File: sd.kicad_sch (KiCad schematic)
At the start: 2 parts, among them J6 Micro_SD_Card_Det1

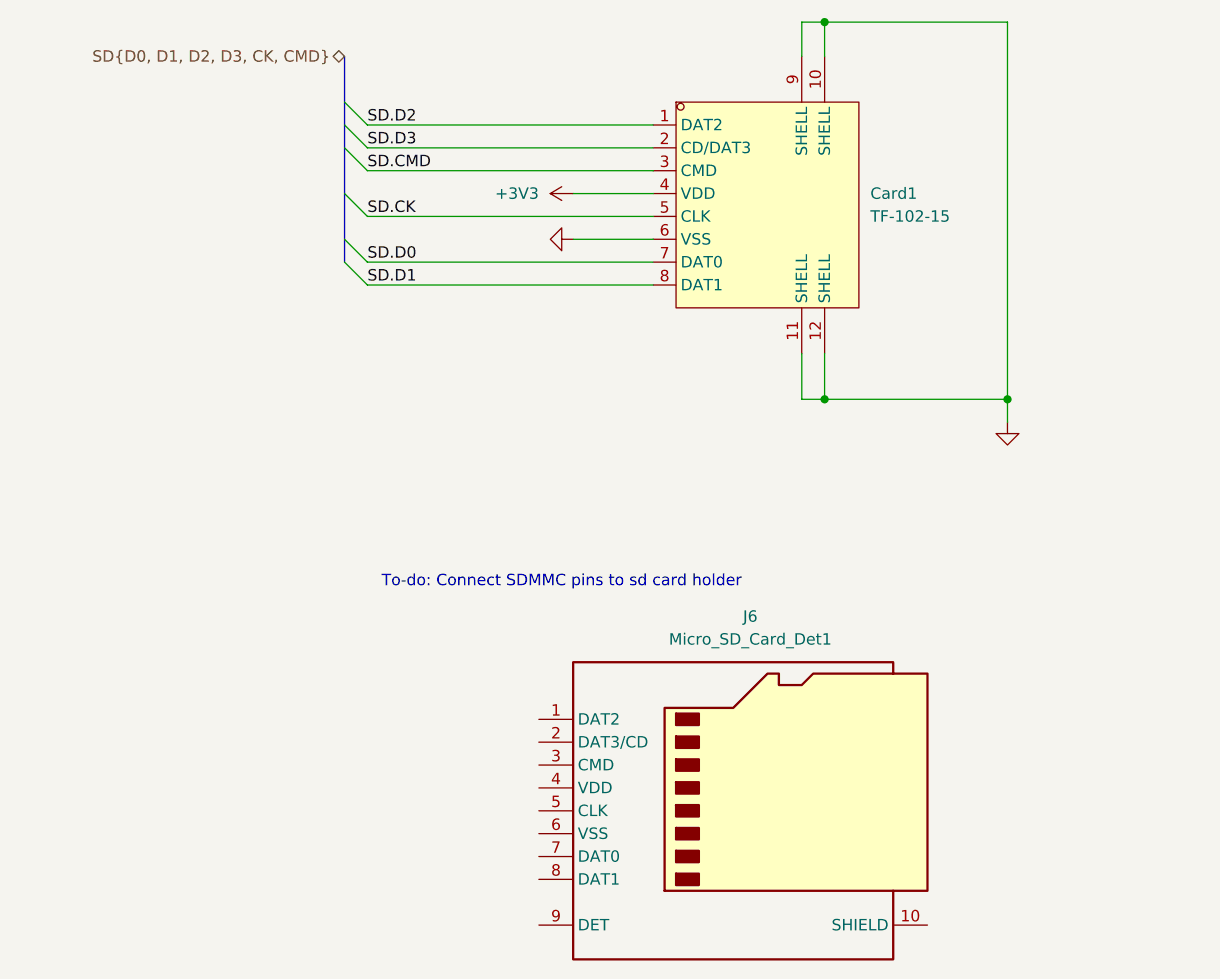
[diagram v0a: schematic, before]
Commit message: added load capacitors to oscillator
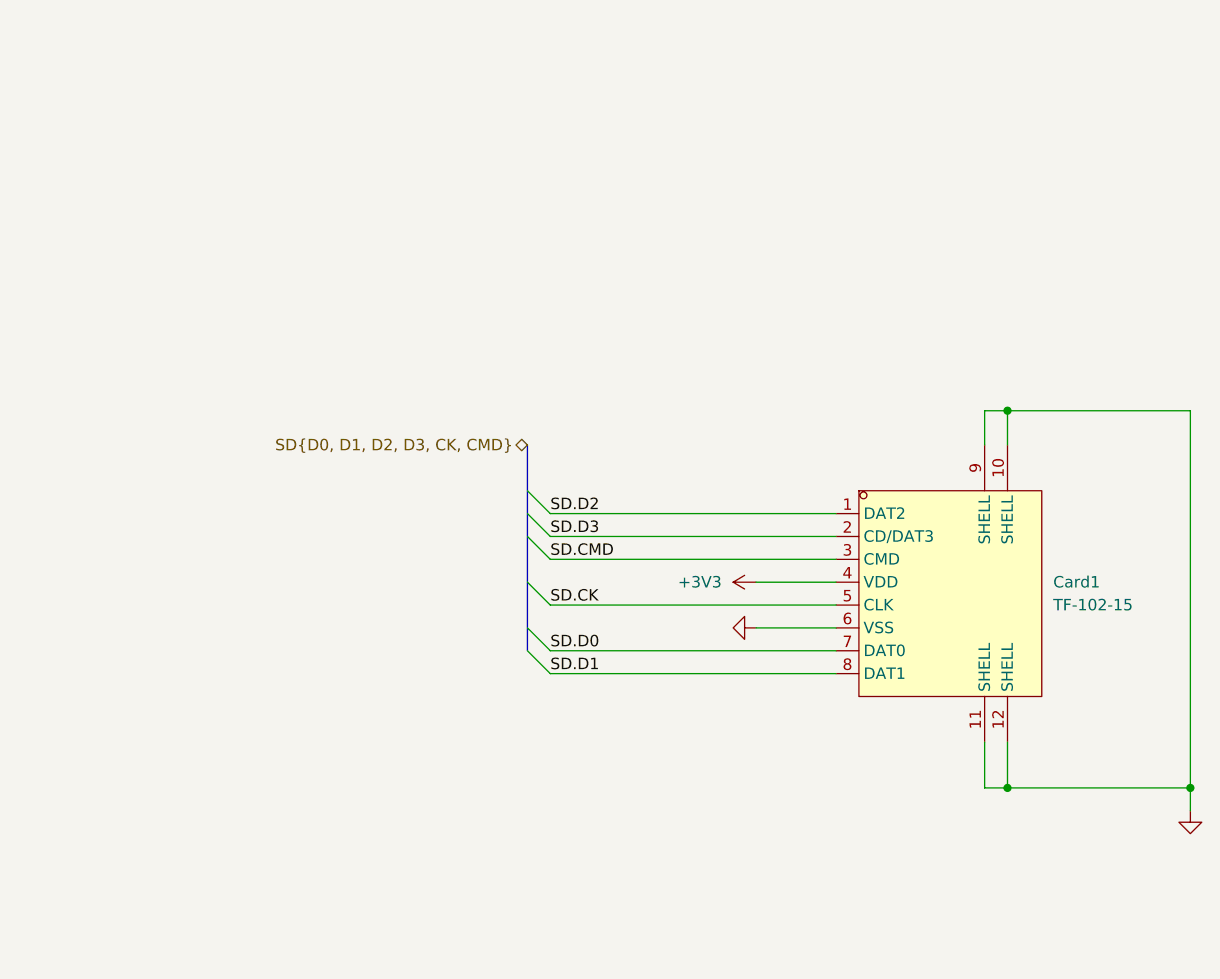
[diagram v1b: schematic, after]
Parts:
- removed J6: Micro_SD_Card_Det1, symbol Connector:Micro_SD_Card_Det1
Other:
- note removed: "To-do: Connect SDMMC pins to sd card holder"
- moved on the sheet: Card1
